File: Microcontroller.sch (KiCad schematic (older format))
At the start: 40 parts, among them CN2 CONN_RCPT_USB2.0_MINI_B_SMD_R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, M1 2N7002BK, M2 2N7002BK, Q10 2N7002BK, U2 STM32L476RGLQFP64, X1 ABM3B-16.000MHZ

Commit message: Update Microcontroller.sch
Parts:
- added JP?: Pin_Header,_1x6-Way,_2.54mm_Pitch, symbol OpenVent:Pin_Header,_1x6-Way,_2.54mm_Pitch
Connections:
- wire segments 183 -> 198
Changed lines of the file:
@@
 Wire Wire Line
 	6350 1900 6550 1900
+$Comp
+L OpenVent:Pin_Header,_1x6-Way,_2.54mm_Pitch JP?
+U 1 1 60546722
+P 1100 1000
+F 0 "JP?" H 1293 825 50  0000 C CNN
+F 1 "Pin_Header,_1x6-Way,_2.54mm_Pitch" H 1300 1500 50  0001 C CNN
+F 2 "" H 1300 1500 50  0001 C CNN
+F 3 "" H 1300 1500 50  0001 C CNN
+	1    1100 1000
+	-1   0    0    1
+$EndComp
+$Comp
+L OpenVent:+3.3V #PWR?
+U 1 1 60547AA4
+P 1100 750
+F 0 "#PWR?" H 1100 600 50  0001 C CNN
+F 1 "+3.3V" H 1100 923 50  0000 C CNN
+F 2 "" H 1100 750 50  0001 C CNN
+F 3 "" H 1100 750 50  0001 C CNN
+	1    1100 750
+	1    0    0    -1
+$EndComp
+$Comp
+L OpenVent:GND #PWR?
+U 1 1 60548A69
+P 1450 850
+F 0 "#PWR?" H 1450 600 50  0001 C CNN
+F 1 "GND" H 1450 700 50  0001 C CNN
+F 2 "" H 1450 850 50  0001 C CNN
+F 3 "" H 1450 850 50  0001 C CNN
+	1    1450 850
+	1    0    0    -1
+$EndComp
+Wire Wire Line
+	1100 1000 1100 750
+Wire Wire Line
+	1100 1100 1250 1100
+Wire Wire Line
+	1450 800  1450 850
+Text GLabel 1450 1200 2    50   Output ~ 0
+SPI1_FPGA_CS
+Text GLabel 1450 1350 2    50   Output ~ 0
+SPI1_MISO
+Text GLabel 1450 1500 2    50   Output ~ 0
+SPI1_MOSI
+Text GLabel 1450 1650 2    50   Output ~ 0
+SPI1_SCLK
+Wire Wire Line
+	1250 1100 1250 800
+Wire Wire Line
+	1250 800  1450 800
+Wire Wire Line
+	1100 1200 1450 1200
+Wire Wire Line
+	1100 1300 1350 1300
+Wire Wire Line
+	1350 1300 1350 1350
+Wire Wire Line
+	1350 1350 1450 1350
+Wire Wire Line
+	1100 1400 1300 1400
+Wire Wire Line
+	1300 1400 1300 1500
+Wire Wire Line
+	1300 1500 1450 1500
+Wire Wire Line
+	1100 1500 1200 1500
+Wire Wire Line
+	1200 1500 1200 1650
+Wire Wire Line
+	1200 1650 1450 1650
 $EndSCHEMATC

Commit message: Update Microcontroller.sch
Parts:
- added TVS-D1, TVS-D2: ESD5Z3.3T1G, SODFL1608X70N, symbol OpenVent:ESD5Z3.3T1G
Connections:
- wire segments 198 -> 209
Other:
- moved on the sheet: JP4, R51, R52
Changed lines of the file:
@@
 Comment4 ""
 $EndDescr
-Text Notes 1925 2850 1    50   ~ 0
+Text Notes 675  2500 1    50   ~ 0
 Debug UART
-Text Notes 1850 3125 0    50   ~ 0
+Text Notes 500  2775 0    50   ~ 0
 Mates with FTDI cable part
 Text GLabel 6550 2900 2    50   Output ~ 0
@@
 L OpenVent:GND #GND_07
 U 1 1 5F8DD179
-P 2875 2450
-F 0 "#GND_07" H 2875 2450 20  0001 C CNN
-F 1 "GND" H 2875 2380 50  0001 C CNN
-F 2 "" H 2875 2450 70  0001 C CNN
-F 3 "" H 2875 2450 70  0001 C CNN
-	1    2875 2450
+P 1625 2100
+F 0 "#GND_07" H 1625 2100 20  0001 C CNN
+F 1 "GND" H 1625 2030 50  0001 C CNN
+F 2 "" H 1625 2100 70  0001 C CNN
+F 3 "" H 1625 2100 70  0001 C CNN
+	1    1625 2100
 	1    0    0    -1
 $EndComp
 Text GLabel 4750 3600 0    50   Input ~ 0
 VBATT-SCALED
-NoConn ~ 2375 2600
+NoConn ~ 1125 2250
 Text GLabel 4750 3500 0    50   Input ~ 0
 MOTOR-CURRENT
@@
 Text Label 4050 2700 0    50   ~ 0
 USART-STM-RX
-NoConn ~ 2375 2500
-NoConn ~ 2375 2900
+NoConn ~ 1125 2150
+NoConn ~ 1125 2550
 $Comp
 L OpenVent:3V3 #3V3_03
@@
 	1    0    0    -1
 $EndComp
-Text Notes 1875 3225 0    50   ~ 0
+Text Notes 525  2875 0    50   ~ 0
 TTL-232R-3V3
 Text GLabel 4750 4000 0    50   Input ~ 0
@@
 	1700 4050 1700 3700
 Wire Wire Line
-	4950 2600 3075 2600
-Wire Wire Line
-	2375 2700 2550 2700
-Wire Wire Line
-	2875 2400 2375 2400
-Wire Wire Line
-	2875 2450 2875 2400
+	1625 2050 1125 2050
+Wire Wire Line
+	1625 2100 1625 2050
 Wire Wire Line
 	4975 6825 4325 6825
@@
 L OpenVent:Pin_Header,_1x6-Way,_2.54mm_Pitch JP4
 U 1 1 5F8DD14A
-P 2375 2900
-F 0 "JP4" H 2725 3550 50  0000 L BNN
-F 1 "Pin_Header,_1x6-Way,_2.54mm_Pitch" H 2375 2900 50  0001 C CNN
-F 2 "Connector_PinHeader_2.54mm:PinHeader_1x06_P2.54mm_Vertical" H 2375 2900 50  0001 C CNN
-F 3 "" H 2375 2900 50  0001 C CNN
-	1    2375 2900
+P 1125 2550
+F 0 "JP4" H 1475 3200 50  0000 L BNN
+F 1 "Pin_Header,_1x6-Way,_2.54mm_Pitch" H 1125 2550 50  0001 C CNN
+F 2 "Connector_PinHeader_2.54mm:PinHeader_1x06_P2.54mm_Vertical" H 1125 2550 50  0001 C CNN
+F 3 "" H 1125 2550 50  0001 C CNN
+	1    1125 2550
 	-1   0    0    -1
 $EndComp
@@
 L OpenVent:33R_Chip_Resistor,_1%,_0.1W R51
 U 1 1 5FF35864
-P 2650 2600
-F 0 "R51" H 2750 2707 50  0000 C CNN
-F 1 "33R_Chip_Resistor,_1%,_0.1W" H 2300 2950 50  0001 C CNN
-F 2 "" H 2850 2600 50  0001 C CNN
-F 3 "" H 2650 2600 50  0001 C CNN
-F 4 "33R" H 2750 2616 50  0000 C CNN "Val"
-F 5 "1%" H 3200 2600 50  0001 C CNN "Tolerance"
-F 6 "0.1W" H 2650 2600 50  0001 C CNN "Watt"
-	1    2650 2600
-	1    0    0    -1
+P 2900 2550
+F 0 "R51" H 3000 2657 50  0000 C CNN
+F 1 "33R_Chip_Resistor,_1%,_0.1W" H 2550 2900 50  0001 C CNN
+F 2 "" H 3100 2550 50  0001 C CNN
+F 3 "" H 2900 2550 50  0001 C CNN
+F 4 "33R" H 3000 2566 50  0000 C CNN "Val"
+F 5 "1%" H 3450 2550 50  0001 C CNN "Tolerance"
+F 6 "0.1W" H 2900 2550 50  0001 C CNN "Watt"
+	1    2900 2550
+	-1   0    0    1
 $EndComp
 $Comp
 L OpenVent:33R_Chip_Resistor,_1%,_0.1W R52
 U 1 1 5FF35DAD
-P 2650 2700
-F 0 "R52" H 2750 2425 50  0000 C CNN
-F 1 "33R_Chip_Resistor,_1%,_0.1W" H 2300 3050 50  0001 C CNN
-F 2 "" H 2850 2700 50  0001 C CNN
-F 3 "" H 2650 2700 50  0001 C CNN
-F 4 "33R" H 2750 2500 50  0000 C CNN "Val"
-F 5 "1%" H 3200 2700 50  0001 C CNN "Tolerance"
-F 6 "0.1W" H 2650 2700 50  0001 C CNN "Watt"
-	1    2650 2700
-	1    0    0    -1
-$EndComp
-Wire Wire Line
-	2550 2800 2375 2800
-Wire Wire Line
-	3075 2600 3075 2800
-Wire Wire Line
-	2950 2800 3075 2800
-Wire Wire Line
-	2950 2700 4950 2700
+P 2900 2450
+F 0 "R52" H 3000 2175 50  0000 C CNN
+F 1 "33R_Chip_Resistor,_1%,_0.1W" H 2550 2800 50  0001 C CNN
+F 2 "" H 3100 2450 50  0001 C CNN
+F 3 "" H 2900 2450 50  0001 C CNN
+F 4 "33R" H 3000 2250 50  0000 C CNN "Val"
+F 5 "1%" H 3450 2450 50  0001 C CNN "Tolerance"
+F 6 "0.1W" H 2900 2450 50  0001 C CNN "Watt"
+	1    2900 2450
+	-1   0    0    1
+$EndComp
 Wire Wire Line
 	6975 6225 6975 6175
@@
 Wire Wire Line
 	1200 1650 1450 1650
+$Comp
+L OpenVent:ESD5Z3.3T1G TVS-D2
+U 1 1 605B29D3
+P 2200 2500
+F 0 "TVS-D2" H 2454 2756 50  0000 C CNN
+F 1 "ESD5Z3.3T1G" H 2520 2677 50  0000 C CNN
+F 2 "SODFL1608X70N" H 2650 2500 50  0001 L CNN
+F 3 "http://www.onsemi.com/pub/Collateral/ESD5Z2.5T1-D.PDF" H 2650 2400 50  0001 L CNN
+F 4 "TVS Diode Uni-Direct. 240W 3.3V SOD-523 ON Semiconductor ESD5Z3.3T1G Uni-Directional TVS Diode, 200W peak, 2-Pin SOD-523" H 2650 2300 50  0001 L CNN "Description"
+F 5 "0.7" H 2650 2200 50  0001 L CNN "Height"
+F 6 "ON Semiconductor" H 2650 2100 50  0001 L CNN "Manufacturer_Name"
+F 7 "ESD5Z3.3T1G" H 2650 2000 50  0001 L CNN "Manufacturer_Part_Number"
+F 8 "863-ESD5Z3.3T1G" H 2650 1900 50  0001 L CNN "Mouser Part Number"
+F 9 "https://www.mouser.co.uk/ProductDetail/ON-Semiconductor/ESD5Z33T1G/?qs=OSf9jACorvaH3Y8oRWEcuQ%3D%3D" H 2650 1800 50  0001 L CNN "Mouser Price/Stock"
+F 10 "ESD5Z3.3T1G" H 2650 1700 50  0001 L CNN "Arrow Part Number"
+F 11 "https://www.arrow.com/en/products/esd5z3.3t1g/on-semiconductor" H 2650 1600 50  0001 L CNN "Arrow Price/Stock"
+	1    2200 2500
+	0    1    1    0
+$EndComp
+$Comp
+L OpenVent:ESD5Z3.3T1G TVS-D1
+U 1 1 605B4E90
+P 1950 2500
+F 0 "TVS-D1" H 2165 2244 50  0000 L TNN
+F 1 "ESD5Z3.3T1G" H 2295 2323 50  0000 C CNN
+F 2 "SODFL1608X70N" H 2400 2500 50  0001 L CNN
+F 3 "http://www.onsemi.com/pub/Collateral/ESD5Z2.5T1-D.PDF" H 2400 2400 50  0001 L CNN
+F 4 "TVS Diode Uni-Direct. 240W 3.3V SOD-523 ON Semiconductor ESD5Z3.3T1G Uni-Directional TVS Diode, 200W peak, 2-Pin SOD-523" H 2400 2300 50  0001 L CNN "Description"
+F 5 "0.7" H 2400 2200 50  0001 L CNN "Height"
+F 6 "ON Semiconductor" H 2400 2100 50  0001 L CNN "Manufacturer_Name"
+F 7 "ESD5Z3.3T1G" H 2400 2000 50  0001 L CNN "Manufacturer_Part_Number"
+F 8 "863-ESD5Z3.3T1G" H 2400 1900 50  0001 L CNN "Mouser Part Number"
+F 9 "https://www.mouser.co.uk/ProductDetail/ON-Semiconductor/ESD5Z33T1G/?qs=OSf9jACorvaH3Y8oRWEcuQ%3D%3D" H 2400 1800 50  0001 L CNN "Mouser Price/Stock"
+F 10 "ESD5Z3.3T1G" H 2400 1700 50  0001 L CNN "Arrow Part Number"
+F 11 "https://www.arrow.com/en/products/esd5z3.3t1g/on-semiconductor" H 2400 1600 50  0001 L CNN "Arrow Price/Stock"
+	1    1950 2500
+	0    1    1    0
+$EndComp
+Wire Wire Line
+	1125 2350 1950 2350
+Wire Wire Line
+	1125 2450 2200 2450
+Wire Wire Line
+	2200 2500 2200 2450
+Connection ~ 2200 2450
+Wire Wire Line
+	1950 2500 1950 2350
+Connection ~ 1950 2350
+Wire Wire Line
+	1950 3100 1950 3150
+Wire Wire Line
+	1950 3150 2100 3150
+Wire Wire Line
+	2200 3150 2200 3100
+$Comp
+L OpenVent:GND #PWR?
+U 1 1 606192F5
+P 2100 3200
+F 0 "#PWR?" H 2100 2950 50  0001 C CNN
+F 1 "GND" H 2100 3050 50  0001 C CNN
+F 2 "" H 2100 3200 50  0001 C CNN
+F 3 "" H 2100 3200 50  0001 C CNN
+	1    2100 3200
+	1    0    0    -1
+$EndComp
+Wire Wire Line
+	2100 3200 2100 3150
+Connection ~ 2100 3150
+Wire Wire Line
+	2100 3150 2200 3150
+Wire Wire Line
+	4950 2600 3300 2600
+Wire Wire Line
+	3300 2350 3300 2600
+Wire Wire Line
+	3000 2350 3300 2350
+Wire Wire Line
+	3200 2450 3200 2700
+Wire Wire Line
+	3000 2450 3200 2450
+Wire Wire Line
+	3200 2700 4950 2700
+Wire Wire Line
+	1950 2350 2600 2350
+Wire Wire Line
+	2200 2450 2600 2450
 $EndSCHEMATC

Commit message: Update Microcontroller.sch
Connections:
- net labels added: PB_MUTE_MCU
- net labels removed: PB_MUTE
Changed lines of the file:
@@
 BUZZER_PWM
 Text GLabel 6500 2500 2    50   Input ~ 0
-PB_MUTE
+PB_MUTE_MCU
 Text GLabel 6500 2600 2    50   Input ~ 0
 PB_PLUS

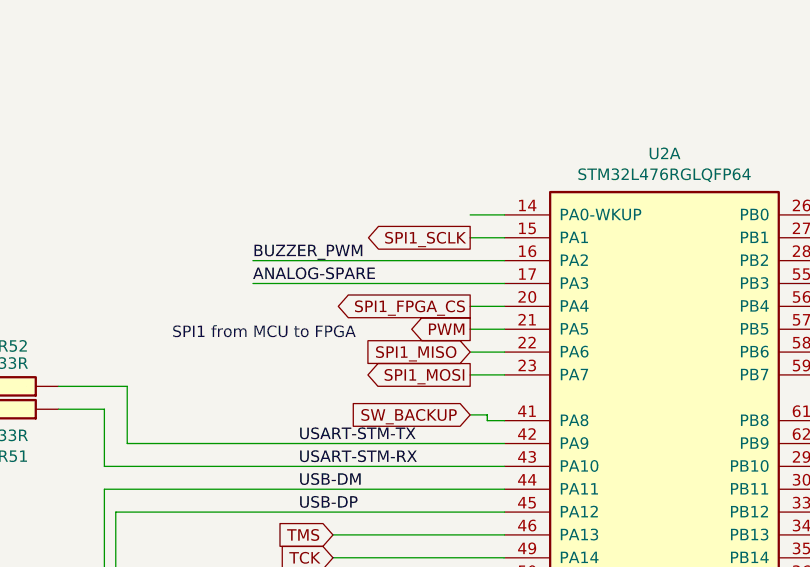
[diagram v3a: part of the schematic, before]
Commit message: PWM and SPI_FPGA_CS pins swapped on MCU
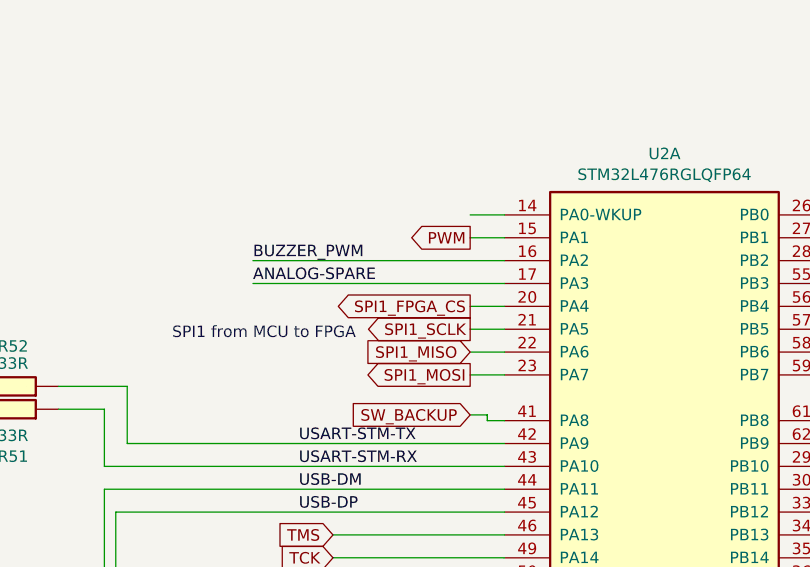
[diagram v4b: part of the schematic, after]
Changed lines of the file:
@@
 Text GLabel 4800 4600 0    50   Input ~ 0
 nPRESSURE-PATIENT-ALERT
-Text GLabel 4800 2100 0    50   Output ~ 0
+Text GLabel 4800 1700 0    50   Output ~ 0
 PWM
 $Comp
@@
 Text GLabel 4800 2000 0    50   Output ~ 0
 SPI1_FPGA_CS
-Text GLabel 4800 1700 0    50   Output ~ 0
+Text GLabel 4800 2100 0    50   Output ~ 0
 SPI1_SCLK
 Wire Wire Line

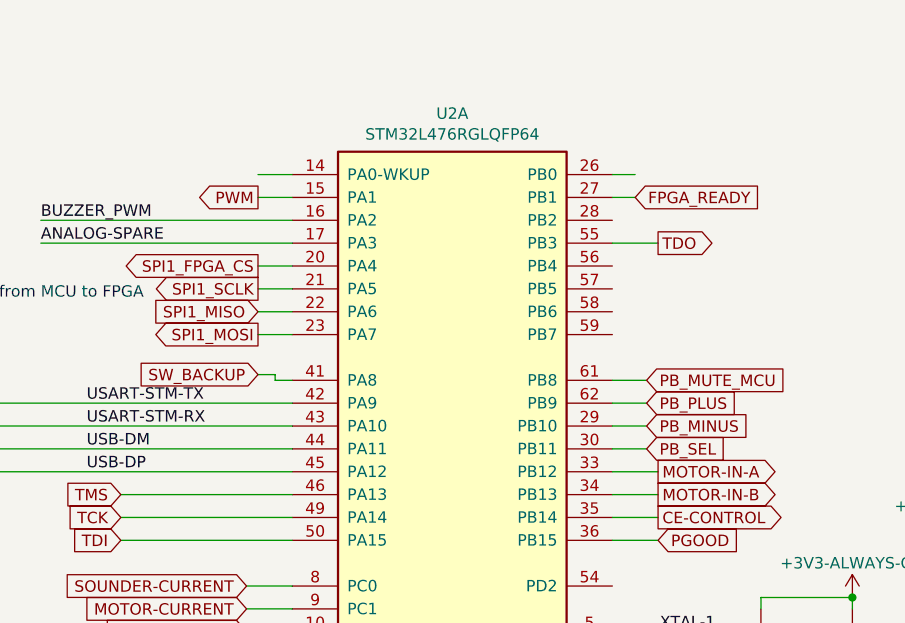
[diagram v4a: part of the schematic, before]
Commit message: Moved PB_SEL from MCU pin PB11 to PA0
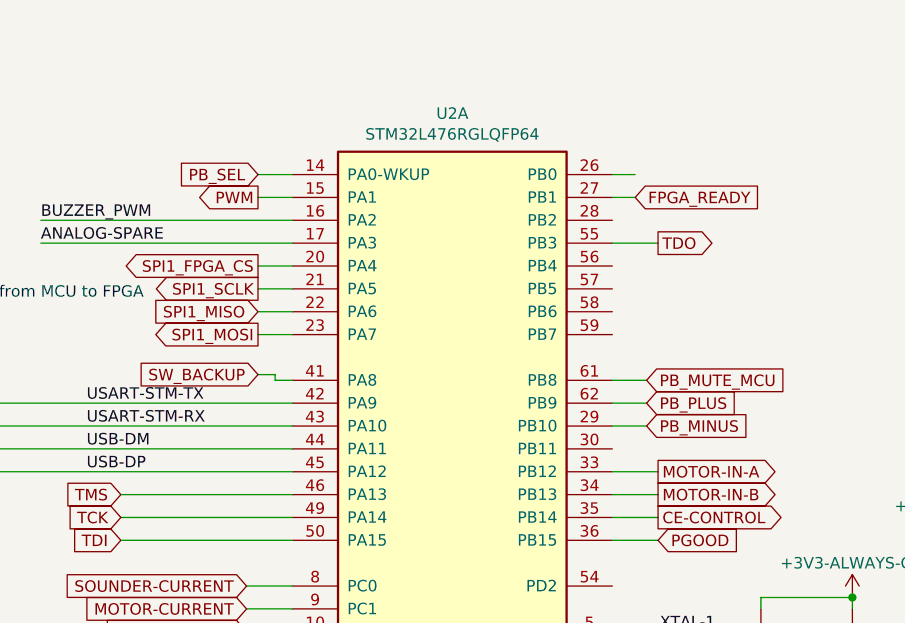
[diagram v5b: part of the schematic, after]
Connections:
- wire segments 209 -> 208
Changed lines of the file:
@@
 	6350 2900 6550 2900
-Wire Wire Line
-	6350 2800 6500 2800
 Wire Wire Line
 	6350 2700 6500 2700
@@
 Text GLabel 6500 2700 2    50   Input ~ 0
 PB_MINUS
-Text GLabel 6500 2800 2    50   Input ~ 0
+Text GLabel 4800 1600 0    50   Input ~ 0
 PB_SEL
 $Comp

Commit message: Update Microcontroller.sch
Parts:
- removed D1(VIN_LED): LED_GREEN_0603_SMD, LED_SMD:LED_0603_1608Metric, symbol OpenVent:LED_GREEN_0603_SMD
- removed M1, M2: 2N7002BK, symbol OpenVent:2N7002BK
- removed R1, R2, R4: 1K_0603_Chip_Resistor,_1%,_0.1W, symbol OpenVent:1K_0603_Chip_Resistor,_1%,_0.1W
- removed R3: 10k_0603_Chip_Resistor,_1%,_0.1W, Resistor_SMD:R_0603_1608Metric, symbol OpenVent:10k_0603_Chip_Resistor,_1%,_0.1W
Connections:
- net labels added: ON
- net labels removed: LDO-EN, VIN_FAIL_FPGA, VIN_FAIL_MCU, nVIN_FAIL
- wire segments 208 -> 184
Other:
- note removed: "Vin_GOOD"
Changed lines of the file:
@@
 Text GLabel 4750 3900 0    50   Input ~ 0
 nMOTOR-FAULT-B
-Text GLabel 4750 4100 0    50   Output ~ 0
-LDO-EN
 $Comp
 L OpenVent:+5V #5V_01
@@
 	1    0    0    -1
 $EndComp
-Text GLabel 4800 4500 0    50   Output ~ 0
+Text GLabel 4800 4500 0    50   Input ~ 0
 PWR_UP
 $Comp
@@
 	4950 4000 4750 4000
 Wire Wire Line
-	4750 4100 4950 4100
-Wire Wire Line
 	4800 2100 4950 2100
 Wire Wire Line
@@
 Text GLabel 4800 1600 0    50   Input ~ 0
 PB_SEL
-$Comp
-L OpenVent:2N7002BK M2
-U 1 1 603E15FB
-P 10100 4100
-F 0 "M2" H 9990 3946 50  0000 R CNN
-F 1 "2N7002BK" H 9990 3855 50  0000 R CNN
-F 2 "" H 10100 4100 50  0000 C CNN
-F 3 "" H 10100 4100 50  0000 C CNN
-	1    10100 4100
-	-1   0    0    -1
-$EndComp
-$Comp
-L OpenVent:2N7002BK M1
-U 1 1 603F9909
-P 10100 3200
-F 0 "M1" H 9990 3046 50  0000 R CNN
-F 1 "2N7002BK" H 9990 2955 50  0000 R CNN
-F 2 "" H 10100 3200 50  0000 C CNN
-F 3 "" H 10100 3200 50  0000 C CNN
-	1    10100 3200
-	-1   0    0    -1
-$EndComp
-$Comp
-L OpenVent:1K_0603_Chip_Resistor,_1%,_0.1W R4
-U 1 1 6042A601
-P 10700 2600
-AR Path="/5F988182/6042A601" Ref="R4"  Part="1"
-AR Path="/5F99D63D/6042A601" Ref="R?"  Part="1"
-F 0 "R4" V 10754 2570 50  0000 L CNN
-F 1 "1K_0603_Chip_Resistor,_1%,_0.1W" H 10700 2600 50  0001 C CNN
-F 2 "" H 10700 2600 60  0001 C CNN
-F 3 "" H 10700 2600 60  0001 C CNN
-F 4 "1K" V 10845 2570 50  0000 L CNN "Val"
-F 5 "1%" H 10700 2600 50  0001 C CNN "Tolerance"
-F 6 "0.1W" H 10700 2600 50  0001 C CNN "Watt"
-	1    10700 2600
-	0    1    -1   0
-$EndComp
-$Comp
-L OpenVent:1K_0603_Chip_Resistor,_1%,_0.1W R2
-U 1 1 60436A21
-P 10600 3750
-AR Path="/5F988182/60436A21" Ref="R2"  Part="1"
-AR Path="/5F99D63D/60436A21" Ref="R?"  Part="1"
-F 0 "R2" V 10654 3720 50  0000 L CNN
-F 1 "1K_0603_Chip_Resistor,_1%,_0.1W" H 10600 3750 50  0001 C CNN
-F 2 "" H 10600 3750 60  0001 C CNN
-F 3 "" H 10600 3750 60  0001 C CNN
-F 4 "1K" V 10745 3720 50  0000 L CNN "Val"
-F 5 "1%" H 10600 3750 50  0001 C CNN "Tolerance"
-F 6 "0.1W" H 10600 3750 50  0001 C CNN "Watt"
-	1    10600 3750
-	1    0    0    -1
-$EndComp
-$Comp
-L OpenVent:10k_0603_Chip_Resistor,_1%,_0.1W R3
-U 1 1 604A9F02
-P 10100 2250
-F 0 "R3" V 10250 2000 50  0000 L BNN
-F 1 "10k_0603_Chip_Resistor,_1%,_0.1W" V 10100 2100 50  0001 C CNN
-F 2 "Resistor_SMD:R_0603_1608Metric" H 10000 2110 50  0001 C CNN
-F 3 "" H 10000 2110 50  0001 C CNN
-F 4 "1%" V 4500 -2750 50  0001 C CNN "Tolerance"
-F 5 "10k" V 10100 2000 50  0000 C CNN "Val"
-F 6 "0.1W" H 10100 2250 50  0001 C CNN "Watt"
-	1    10100 2250
-	0    -1   -1   0
-$EndComp
-Text GLabel 9550 3450 0    50   Input ~ 0
-nVIN_FAIL
-Text GLabel 10550 3050 2    50   Output ~ 0
-VIN_FAIL_MCU
-$Comp
-L OpenVent:GND #GND_?
-U 1 1 606DD025
-P 10100 4850
-F 0 "#GND_?" H 10100 4600 50  0001 C CNN
-F 1 "GND" H 10100 4700 50  0001 C CNN
-F 2 "" H 10100 4850 50  0000 C CNN
-F 3 "" H 10100 4850 50  0000 C CNN
-	1    10100 4850
-	1    0    0    -1
-$EndComp
-$Comp
-L OpenVent:GND #GND_?
-U 1 1 6071B931
-P 10100 3700
-F 0 "#GND_?" H 10100 3450 50  0001 C CNN
-F 1 "GND" H 10100 3550 50  0001 C CNN
-F 2 "" H 10100 3700 50  0000 C CNN
-F 3 "" H 10100 3700 50  0000 C CNN
-	1    10100 3700
-	1    0    0    -1
-$EndComp
-Wire Wire Line
-	10100 3600 10100 3700
-Wire Wire Line
-	10600 2700 10600 2800
-Wire Wire Line
-	10100 3050 10100 3200
-Wire Wire Line
-	10600 2300 10600 2250
-$Comp
-L OpenVent:+3V3-ALWAYS-ON #PWR?
-U 1 1 60842A63
-P 10600 1500
-F 0 "#PWR?" H 10600 1400 50  0001 C CNN
-F 1 "+3V3-ALWAYS-ON" H 10600 1673 50  0000 C CNN
-F 2 "" H 10600 1500 50  0001 C CNN
-F 3 "" H 10600 1500 50  0001 C CNN
-	1    10600 1500
-	1    0    0    -1
-$EndComp
-$Comp
-L OpenVent:+3.3V #PWR?
-U 1 1 608506F9
-P 10900 3750
-F 0 "#PWR?" H 10900 3600 50  0001 C CNN
-F 1 "+3.3V" H 10900 3923 50  0000 C CNN
-F 2 "" H 10900 3750 50  0001 C CNN
-F 3 "" H 10900 3750 50  0001 C CNN
-	1    10900 3750
-	1    0    0    -1
-$EndComp
-Wire Wire Line
-	10900 3850 10900 3750
-Text GLabel 10500 4100 2    50   Output ~ 0
-VIN_FAIL_FPGA
-Wire Wire Line
-	10500 3850 10350 3850
-Wire Wire Line
-	10350 3850 10350 4100
-Wire Wire Line
-	10350 4100 10500 4100
-Wire Wire Line
-	9700 4350 9800 4350
-$Comp
-L OpenVent:GND #GND_?
-U 1 1 6071A6F8
-P 9700 4850
-F 0 "#GND_?" H 9700 4600 50  0001 C CNN
-F 1 "GND" H 9700 4700 50  0001 C CNN
-F 2 "" H 9700 4850 50  0000 C CNN
-F 3 "" H 9700 4850 50  0000 C CNN
-	1    9700 4850
-	1    0    0    -1
-$EndComp
-$Comp
-L OpenVent:1K_0603_Chip_Resistor,_1%,_0.1W R1
-U 1 1 6045AB44
-P 9800 4500
-AR Path="/5F988182/6045AB44" Ref="R1"  Part="1"
-AR Path="/5F99D63D/6045AB44" Ref="R?"  Part="1"
-F 0 "R1" V 9854 4470 50  0000 L CNN
-F 1 "1K_0603_Chip_Resistor,_1%,_0.1W" H 9800 4500 50  0001 C CNN
-F 2 "" H 9800 4500 60  0001 C CNN
-F 3 "" H 9800 4500 60  0001 C CNN
-F 4 "1K" V 9945 4470 50  0000 L CNN "Val"
-F 5 "1%" H 9800 4500 50  0001 C CNN "Tolerance"
-F 6 "0.1W" H 9800 4500 50  0001 C CNN "Watt"
-	1    9800 4500
-	0    1    1    0
-$EndComp
-Wire Wire Line
-	9550 3450 9700 3450
-Wire Wire Line
-	10100 4100 10350 4100
-Connection ~ 10350 4100
-Wire Wire Line
-	9700 4350 9700 3450
-Connection ~ 9700 3450
-Wire Wire Line
-	9700 3450 9800 3450
-Wire Wire Line
-	10100 4500 10100 4850
-Wire Wire Line
-	10200 2350 10200 2800
-Wire Wire Line
-	10600 2800 10200 2800
-Wire Wire Line
-	10200 1950 10200 1650
-Wire Wire Line
-	10200 1650 10600 1650
-Wire Wire Line
-	10600 1500 10600 1650
-Text Notes 10800 2000 0    50   ~ 0
-Vin_GOOD
-Wire Wire Line
-	9700 4850 9700 4800
-Wire Wire Line
-	9700 4400 9700 4350
-Connection ~ 9700 4350
-Wire Wire Line
-	10100 3050 10200 3050
-Wire Wire Line
-	10200 2800 10200 3050
-Connection ~ 10200 2800
-Connection ~ 10200 3050
-Wire Wire Line
-	10200 3050 10550 3050
-Connection ~ 10600 1650
-$Comp
-L OpenVent:LED_GREEN_0603_SMD D?
-U 1 1 604063DB
-P 10600 1650
-AR Path="/604063DB" Ref="D?"  Part="1"
-AR Path="/5F988182/604063DB" Ref="D1(VIN_LED)"  Part="1"
-F 0 "D1(VIN_LED)" V 10790 1760 50  0000 L BNN
-F 1 "LED_GREEN_0603_SMD" V 10890 1760 60  0001 C CNN
-F 2 "LED_SMD:LED_0603_1608Metric" H 10890 1760 50  0001 C CNN
-F 3 "https://www.rohm.com/datasheet/SML-D12M8W(C)/sml-d12x8(c)-e" H 10890 1760 50  0001 C CNN
-F 4 "" V 10900 1900 50  0000 C CNN "Val"
-F 5 "GREEN" H 10600 1650 50  0001 C CNN "Colour"
-F 6 "SML-D12M8WT86C" H 10600 1650 50  0001 C CNN "Mfr_PN"
-F 7 "LED YELLOW/GREEN 1608 SMD" H 10600 1650 50  0001 C CNN "Desc"
-F 8 "Yellow-Green 572nm LED Indication - Discrete 2.2V 0603 (1608 Metric)" H 10600 1650 50  0001 C CNN "Detailed"
-F 9 "DigiKey" H 10600 1650 50  0001 C CNN "DistName"
-F 10 "SML-D12M8WT86CTR-ND" H 10600 1650 50  0001 C CNN "Dist_PN"
-F 11 "Rohm Semiconductor" H 10600 1650 50  0001 C CNN "Mfr"
-	1    10600 1650
-	0    1    1    0
-$EndComp
-Text Notes 8250 4150 0    50   ~ 0
+Text Notes 7750 4300 0    50   ~ 0
 nRESET leftover from SWD,\nto be replaced with JTAG nRST\nsignal. LM 09/03/21\n\nJTAG/SWD nRST has been added \nKA 15/03/21\n
 Text GLabel 6450 1700 2    50   Input ~ 0
@@
 Wire Wire Line
 	2200 2450 2600 2450
+Wire Wire Line
+	4750 4100 4950 4100
+Text GLabel 4750 4100 0    50   Output ~ 0
+ON
 $EndSCHEMATC
